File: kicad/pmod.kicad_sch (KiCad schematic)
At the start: 25 parts, among them J3 Conn_02x06_Odd_Even, J4 Conn_02x06_Odd_Even, J6 Conn_01x08_Socket, U13 NCP1529A, U14 NCP1529A, U6 LFE5U-85F-6BG381x, U8 LP5907MFX-2.5, X1 ECS-2520MV-500-BL-TR

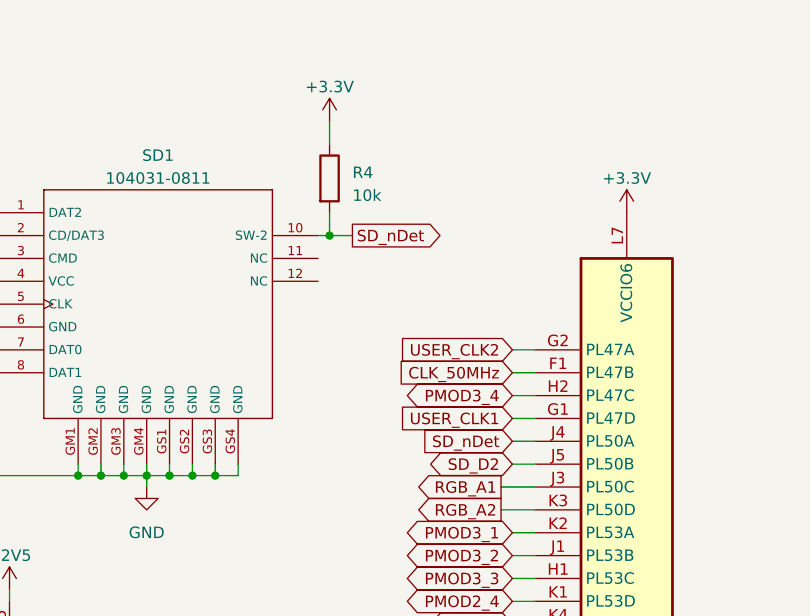
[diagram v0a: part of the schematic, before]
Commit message: Removed the nDet from the SD-card and added the 12 MHz oscillator as clock input to be fully compatible with the GECKO4 clock inputs
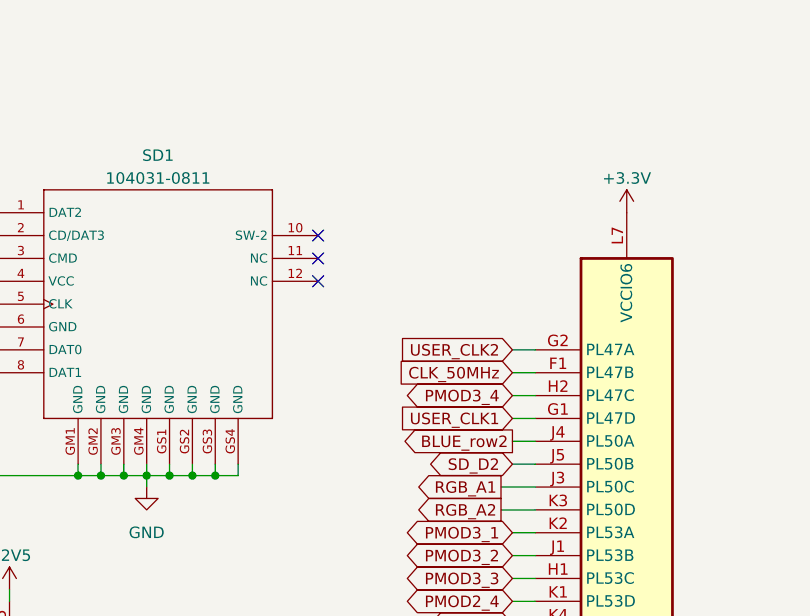
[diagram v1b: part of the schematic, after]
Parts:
- removed R4: 10k, Resistor_SMD:R_0402_1005Metric, symbol Device:R
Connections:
- net SD_nDet: no longer names the net of SD1.10 (SW-2)
- net SD_nDet: no longer U6.J4 (PL50A)
- new net BLUE_row2: U6.J4 (PL50A)
- no-connect marks 1 -> 4
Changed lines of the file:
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@@
   (junction (at 49.53 138.43) (diameter 0) (color 0 0 0 0)
   )
-  (junction (at 220.98 38.1) (diameter 0) (color 0 0 0 0)
-  )
   (junction (at 96.52 119.38) (diameter 0) (color 0 0 0 0)
   )
@@
   )
   (no_connect (at 243.84 91.44))
+  (no_connect (at 219.71 38.1))
+  (no_connect (at 219.71 43.18))
+  (no_connect (at 219.71 40.64))
   (wire (pts (xy 49.53 135.89) (xy 49.53 138.43))
     (stroke (width 0) (type default))
@@
     (stroke (width 0) (type default))
   )
-  (wire (pts (xy 220.98 38.1) (xy 219.71 38.1))
-    (stroke (width 0) (type default))
-  )
   (wire (pts (xy 64.77 114.3) (xy 64.77 119.38))
     (stroke (width 0) (type default))
@@
     (stroke (width 0) (type default))
   )
-  (wire (pts (xy 220.98 35.56) (xy 220.98 38.1))
-    (stroke (width 0) (type default))
-  )
   (wire (pts (xy 50.8 20.32) (xy 62.23 20.32))
     (stroke (width 0) (type default))
@@
     (stroke (width 0) (type default))
   )
-  (wire (pts (xy 220.98 38.1) (xy 223.52 38.1))
-    (stroke (width 0) (type default))
-  )
   (wire (pts (xy 241.3 101.6) (xy 243.84 101.6))
     (stroke (width 0) (type default))
@@
   )
   (wire (pts (xy 120.65 35.56) (xy 123.19 35.56))
-    (stroke (width 0) (type default))
-  )
-  (wire (pts (xy 220.98 25.4) (xy 220.98 27.94))
     (stroke (width 0) (type default))
   )
@@
     )
   )
-  (global_label "SD_nDet" (shape output) (at 223.52 38.1 0) (fields_autoplaced)
-    (effects (font (size 1.27 1.27)) (justify left))
-    (property "Intersheetrefs" "${INTERSHEET_REFS}" (at 234.1062 38.1 0)
-      (effects (font (size 1.27 1.27)) (justify left) hide)
-    )
-  )
   (global_label "PMOD3_1" (shape bidirectional) (at 116.84 82.55 180) (fields_autoplaced)
     (effects (font (size 1.27 1.27)) (justify right))
@@
     )
   )
-  (global_label "SD_nDet" (shape input) (at 241.3 60.96 180) (fields_autoplaced)
-    (effects (font (size 1.27 1.27)) (justify right))
-    (property "Intersheetrefs" "${INTERSHEET_REFS}" (at 230.7138 60.96 0)
-      (effects (font (size 1.27 1.27)) (justify right) hide)
-    )
-  )
   (global_label "SD_D0" (shape bidirectional) (at 171.45 50.8 180) (fields_autoplaced)
     (effects (font (size 1.27 1.27)) (justify right))
@@
     (effects (font (size 1.27 1.27)) (justify right))
     (property "Intersheetrefs" "${INTERSHEET_REFS}" (at 228.5744 99.06 0)
+      (effects (font (size 1.27 1.27)) (justify right) hide)
+    )
+  )
+  (global_label "BLUE_row2" (shape output) (at 241.3 60.96 180) (fields_autoplaced)
+    (effects (font (size 1.27 1.27)) (justify right))
+    (property "Intersheetrefs" "${INTERSHEET_REFS}" (at 228.1738 60.96 0)
       (effects (font (size 1.27 1.27)) (justify right) hide)
     )
@@
     )
   )
-  (symbol (lib_id "Device:R") (at 220.98 31.75 0) (unit 1)
-    (in_bom yes) (on_board yes) (dnp no) (fields_autoplaced)
-    (property "Reference" "R4" (at 223.52 31.115 0)
-      (effects (font (size 1.27 1.27)) (justify left))
-    )
-    (property "Value" "10k" (at 223.52 33.655 0)
-      (effects (font (size 1.27 1.27)) (justify left))
-    )
-    (property "Footprint" "Resistor_SMD:R_0402_1005Metric" (at 219.202 31.75 90)
-      (effects (font (size 1.27 1.27)) hide)
-    )
-    (property "Datasheet" "~" (at 220.98 31.75 0)
-      (effects (font (size 1.27 1.27)) hide)
-    )
-    (pin "1")
-    (pin "2")
-    (instances
-      (project "gecko5education"
-        (path "/47d58937-9286-45a8-b88f-d3fcc6f916c8"
-          (reference "R4") (unit 1)
-        )
-        (path "/47d58937-9286-45a8-b88f-d3fcc6f916c8/2168b384-5196-4073-b8ef-3119545e18e5"
-          (reference "R4") (unit 1)
-        )
-        (path "/47d58937-9286-45a8-b88f-d3fcc6f916c8/e8cfb843-efab-422d-aa9c-640a59ac0396"
-          (reference "R31") (unit 1)
-        )
-      )
-    )
-  )
   (symbol (lib_id "power:GND") (at 194.31 139.7 0) (unit 1)
     (in_bom yes) (on_board yes) (dnp no) (fields_autoplaced)
@@
         )
       )
-    )
-  )
-  (symbol (lib_id "power:+3.3V") (at 220.98 25.4 0) (unit 1)
-    (in_bom yes) (on_board yes) (dnp no) (fields_autoplaced)
-    (property "Reference" "#PWR056" (at 220.98 29.21 0)
-      (effects (font (size 1.27 1.27)) hide)
-    )
-    (property "Value" "+3.3V" (at 220.98 21.59 0)
-      (effects (font (size 1.27 1.27)))
-    )
-    (property "Footprint" "" (at 220.98 25.4 0)
-      (effects (font (size 1.27 1.27)) hide)
-    )
-    (property "Datasheet" "" (at 220.98 25.4 0)
-      (effects (font (size 1.27 1.27)) hide)
-    )
-    (pin "1")
-    (instances
-      (project "gecko5education"
-        (path "/47d58937-9286-45a8-b88f-d3fcc6f916c8/e8cfb843-efab-422d-aa9c-640a59ac0396"
-          (reference "#PWR056") (unit 1)
-        )
-      )
